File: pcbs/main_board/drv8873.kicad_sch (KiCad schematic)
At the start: 10 parts, among them U3 DRV8873HPWPRQ1

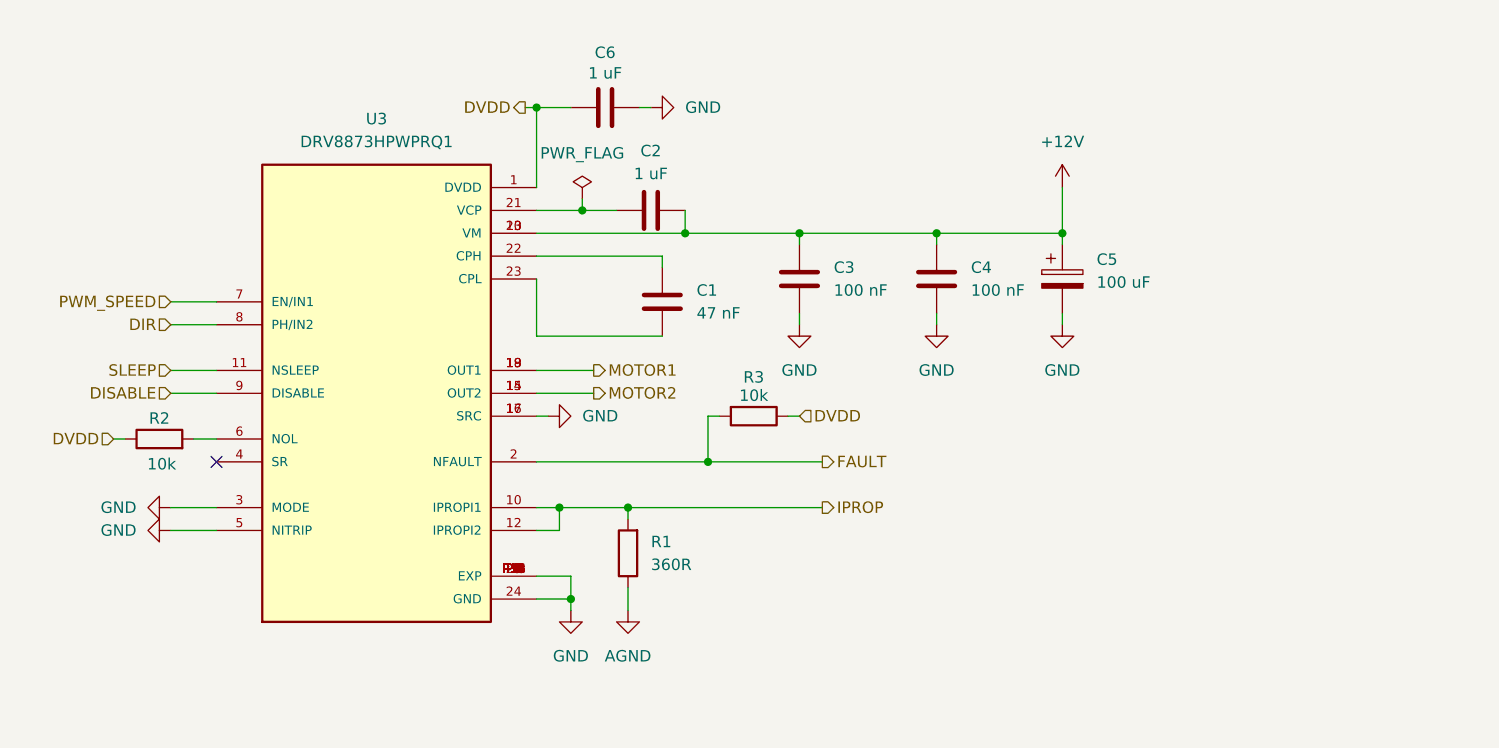
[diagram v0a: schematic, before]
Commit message: Add power distribution sheet
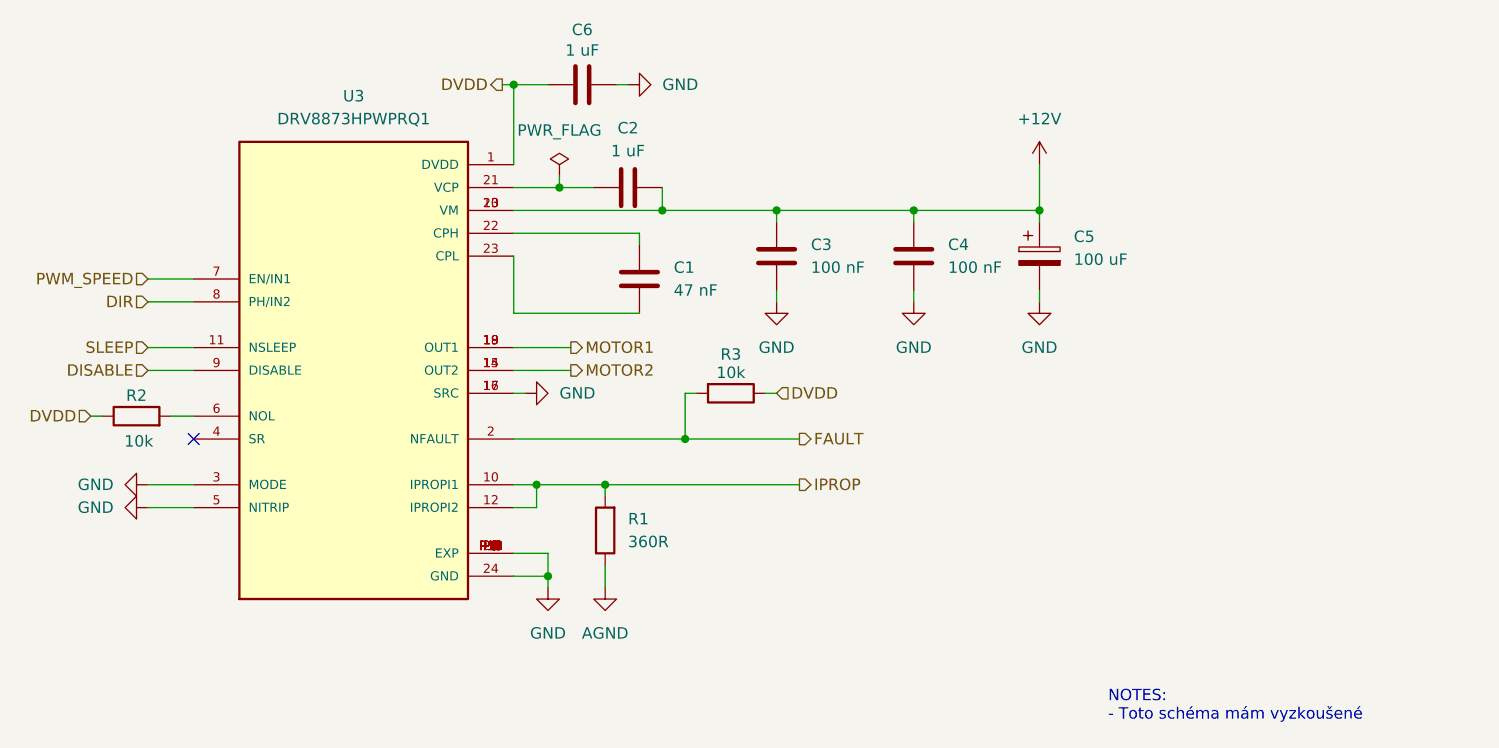
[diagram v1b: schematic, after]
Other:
- note added: "NOTES: - Toto schéma mám vyzkoušené"
- moved on the sheet: C1, C2, C3, C4, C5, C6, R1, R2, R3, U3

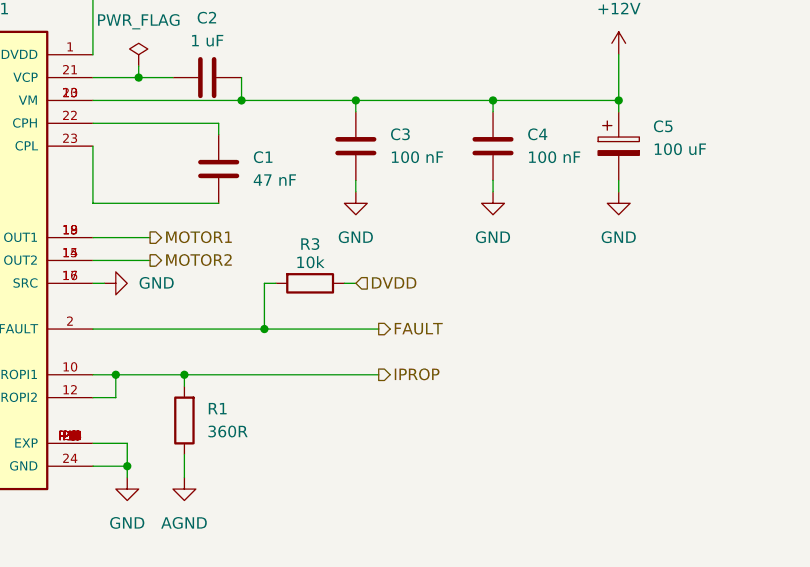
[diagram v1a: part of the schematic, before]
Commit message: wire m driver to esp
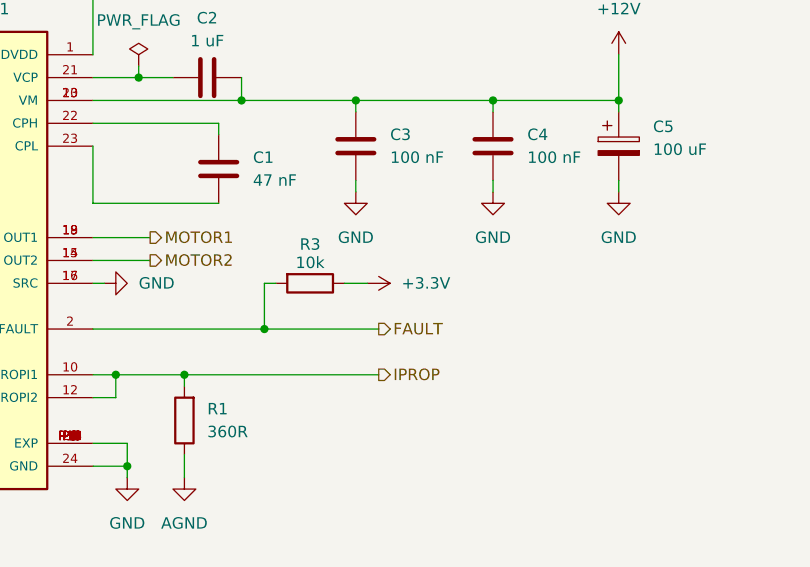
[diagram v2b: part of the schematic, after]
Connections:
- net DVDD: no longer R3.1
- new net +3.3V: R3.1
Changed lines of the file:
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@@
 	(wire
 		(pts
-			(xy 121.92 62.23) (xy 123.19 62.23)
+			(xy 121.92 62.23) (xy 124.46 62.23)
 		)
 		(stroke
@@
 			)
 			(justify right)
-		)
-	)
-	(hierarchical_label "DVDD"
-		(shape input)
-		(at 123.19 62.23 0)
-		(effects
-			(font
-				(size 1.27 1.27)
-			)
-			(justify left)
 		)
 	)
@@
 					(unit 1)
 				)
+			)
+		)
+	)
+	(symbol
+		(lib_id "power:VCC")
+		(at 124.46 62.23 270)
+		(unit 1)
+		(exclude_from_sim no)
+		(in_bom yes)
+		(on_board yes)
+		(dnp no)
+		(fields_autoplaced yes)
+		(property "Reference" "#PWR033"
+			(at 120.65 62.23 0)
+			(effects
+				(font
+					(size 1.27 1.27)
+				)
+				(hide yes)
+			)
+		)
+		(property "Value" "+3.3V"
+			(at 128.27 62.2299 90)
+			(effects
+				(font
+					(size 1.27 1.27)
+				)
+				(justify left)
+			)
+		)
+		(property "Footprint" ""
+			(at 124.46 62.23 0)
+			(effects
+				(font
+					(size 1.27 1.27)
+				)
+				(hide yes)
+			)
+		)
+		(property "Datasheet" ""
+			(at 124.46 62.23 0)
+			(effects
+				(font
+					(size 1.27 1.27)
+				)
+				(hide yes)
+			)
+		)
+		(property "Description" "Power symbol creates a global label with name \"VCC\""
+			(at 124.46 62.23 0)
+			(effects
+				(font
+					(size 1.27 1.27)
+				)
+				(hide yes)
+			)
+		)
+		(pin "1"
+		)
+		(instances
+			(project "main_board"
+				(path "/86b00c07-962a-4c6d-8d05-813891e412c9/42661c25-a76d-41a1-8ad4-79781b4adf06"
+					(reference "#PWR033")
+					(unit 1)
+				)

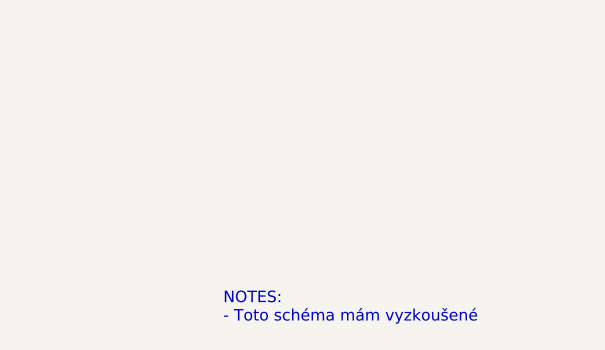
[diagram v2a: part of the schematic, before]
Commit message: ESP power update
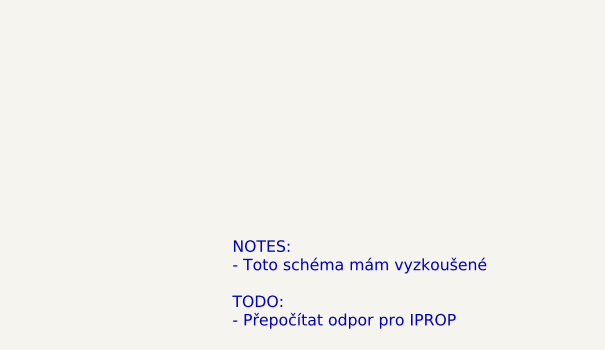
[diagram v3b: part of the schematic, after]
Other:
- note added: "NOTES: - Toto schéma mám vyzkoušené TODO: - Přepočítat odpor pro IPROP"
- note removed: "NOTES: - Toto schéma mám vyzkoušené"
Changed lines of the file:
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@@
 	(generator_version "9.0")
 	(paper "A5")
-	(text "NOTES:\n- Toto schéma mám vyzkoušené"
+	(text "NOTES:\n- Toto schéma mám vyzkoušené\n\nTODO:\n- Přepočítat odpor pro IPROP "
 		(exclude_from_sim no)
-		(at 160.02 95.25 0)
+		(at 161.036 89.662 0)
 		(effects
 			(font

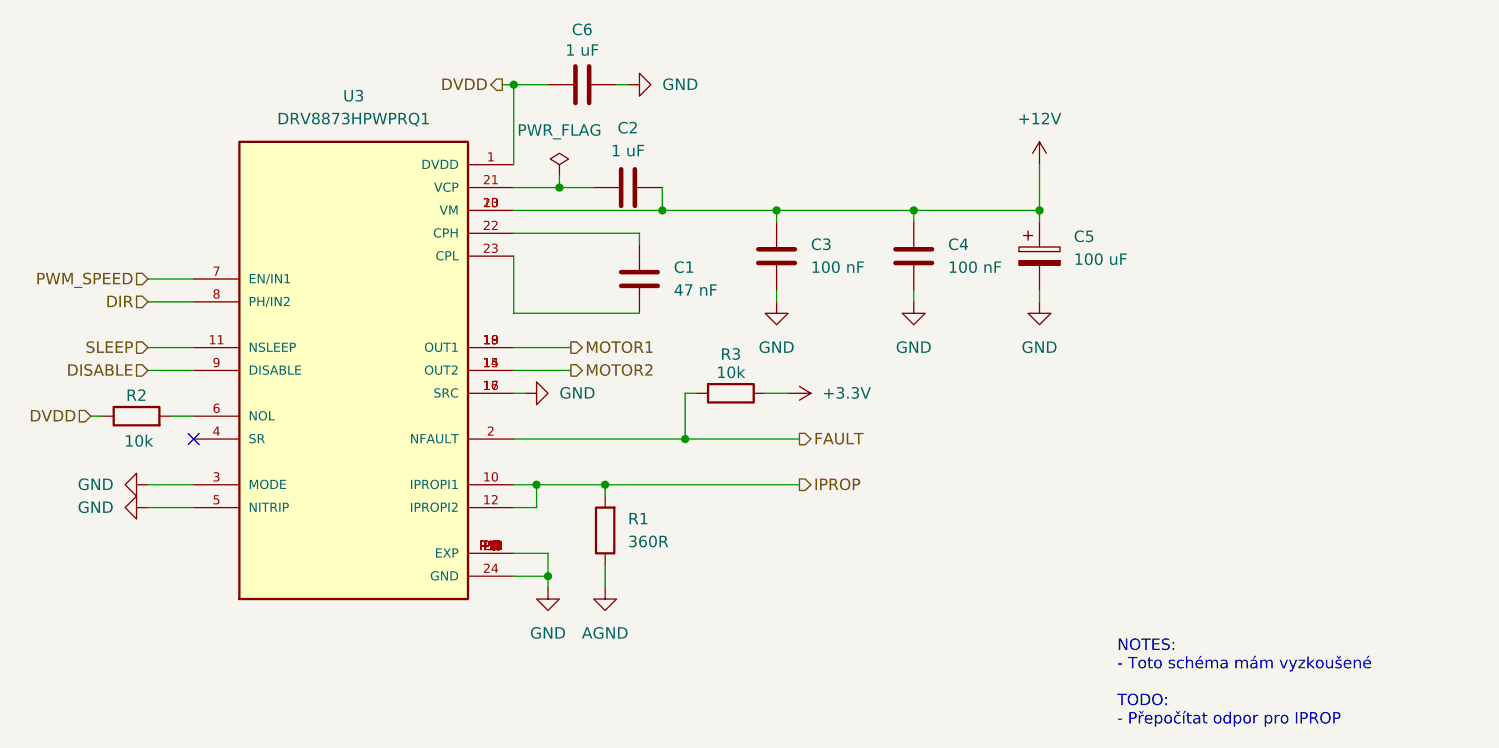
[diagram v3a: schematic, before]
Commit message: Add edge cuts and notes to pcb
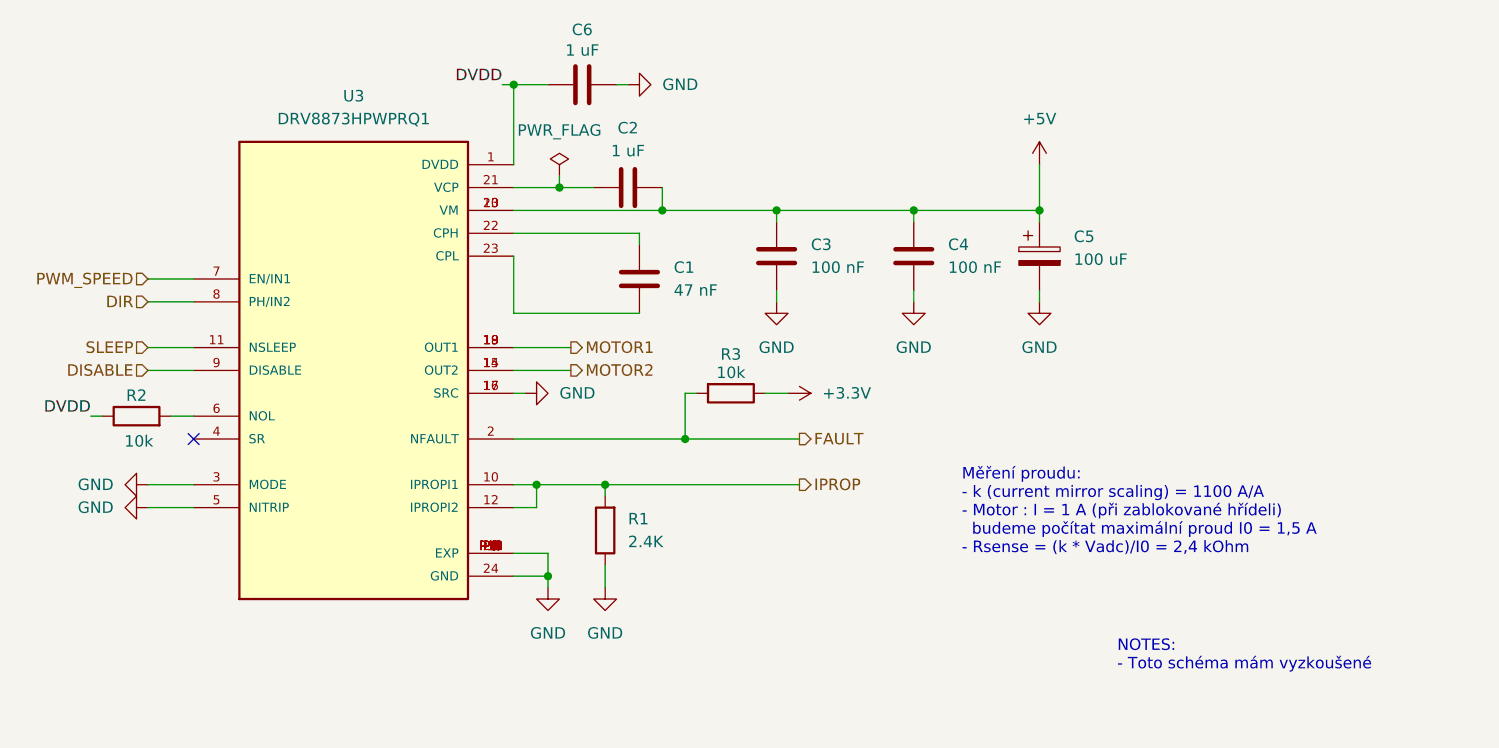
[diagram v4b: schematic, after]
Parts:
- R1: value 360R -> 2.4K; Manufacturer Part Number CRCW0603360RJNTA -> AR0603JR-072K4L; Supplier Part Number 71-CRCW0603J-360 -> 603-AR0603JR-072K4L
- U3: A1_MAX (none) -> None; A1_MIN (none) -> 0.05; A1_NOM (none) -> None; A_MAX (none) -> 1.2; A_MIN (none) -> 1.2; A_NOM (none) -> 1.2; Availability (none) -> In Stock; B_MAX (none) -> 0.3; B_MIN (none) -> 0.19; B_NOM (none) -> 0.245; Check_prices (none) -> https://www.snapeda.com/parts/DRV8873HPWPRQ1/Texas+Instrume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; D2_MAX (none) -> 4.5; D2_MIN (none) -> None; D2_NOM (none) -> None; D_MAX (none) -> 7.9; D_MIN (none) -> 7.7; D_NOM (none) -> 7.8; Description_1 (none) -> Automotive 40-V, 10-A H-bridge motor driver with integrated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; E1_MAX (none) -> 4.5; E1_MIN (none) -> 43.0; E1_NOM (none) -> 23.75; E2_MAX (none) -> 3.0; E2_MIN (none) -> None; E2_NOM (none) -> None; ENOM (none) -> 0.65; E_MAX (none) -> 6.6; E_MIN (none) -> 6.2; E_NOM (none) -> 6.4; L_MAX (none) -> 0.75; L_MIN (none) -> 0.5; L_NOM (none) -> 0.625; MANUFACTURER (none) -> Texas Instruments; MF (none) -> Texas Instruments; MP (none) -> DRV8873HPWPRQ1; PARTREV (none) -> AUG2018; PIN_COUNT (none) -> 24.0; Package (none) -> HTSSOP-24 Texas Instruments; Price (none) -> None; STANDARD (none) -> IPC 7351B; SnapEDA_Link (none) -> https://www.snapeda.com/parts/DRV8873HPWPRQ1/Texas+Instrume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
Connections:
- net AGND is gone; now on net GND: R1.1
- net +12V renamed +5V
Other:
- note added: "Měření proudu: - k (current mirror scaling) = 1100 A/A - Motor : I = 1 A (při zablokované hřídeli) budeme počítat maximální proud I0 = 1,5 A - Rsense = (k * Vadc)/I0 = 2,4 kOhm"
- note added: "NOTES: - Toto schéma mám vyzkoušené"
- note removed: "NOTES: - Toto schéma mám vyzkoušené TODO: - Přepočítat odpor pro IPROP"

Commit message: Components update
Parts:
- U3: A1_MAX None -> (none); A1_MIN 0.05 -> (none); A1_NOM None -> (none); A_MAX 1.2 -> (none); A_MIN 1.2 -> (none); A_NOM 1.2 -> (none); Availability In Stock -> (none); B_MAX 0.3 -> (none); B_MIN 0.19 -> (none); B_NOM 0.245 -> (none); Check_prices https://www.snapeda.com/parts/DRV8873HPWPRQ1/Texas+Instrume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 -> (none); D2_MAX 4.5 -> (none); D2_MIN None -> (none); D2_NOM None -> (none); D_MAX 7.9 -> (none); D_MIN 7.7 -> (none); D_NOM 7.8 -> (none); Description_1 Automotive 40-V, 10-A H-bridge motor driver with integrated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 -> (none); E1_MAX 4.5 -> (none); E1_MIN 43.0 -> (none); E1_NOM 23.75 -> (none); E2_MAX 3.0 -> (none); E2_MIN None -> (none); E2_NOM None -> (none); ENOM 0.65 -> (none); E_MAX 6.6 -> (none); E_MIN 6.2 -> (none); E_NOM 6.4 -> (none); L_MAX 0.75 -> (none); L_MIN 0.5 -> (none); L_NOM 0.625 -> (none); MANUFACTURER Texas Instruments -> (none); MF Texas Instruments -> (none); MP DRV8873HPWPRQ1 -> (none); PARTREV AUG2018 -> (none); PIN_COUNT 24.0 -> (none); Package HTSSOP-24 Texas Instruments -> (none); Price None -> (none); STANDARD IPC 7351B -> (none); SnapEDA_Link https://www.snapeda.com/parts/DRV8873HPWPRQ1/Texas+Instrume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 -> (none)

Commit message: Main board final update
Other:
- note removed: "NOTES: - Toto schéma mám vyzkoušené"
- company: (none) -> Brno Mars Rover
- title: (none) -> Main board - MyMachine LED cap
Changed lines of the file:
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@@
 	(generator "eeschema")
 	(generator_version "9.0")
-	(paper "A5")
+	(paper "A4")
+	(title_block
+		(title "Main board - MyMachine LED cap")
+		(date "2026-01-20")
+		(company "Brno Mars Rover")
+	)
 	(text "Měření proudu:\n- k (current mirror scaling) = 1100 A/A\n- Motor : I = 1 A (při zablokované hřídeli)\n  budeme počítat maximální proud I0 = 1,5 A\n- Rsense = (k * Vadc)/I0 = 2,4 kOhm"
 		(exclude_from_sim no)
@@
 		(effects
 			(font
-				(size 1.27 1.27)
-			)
-			(justify left top)
-		)
-	)
-	(text "NOTES:\n- Toto schéma mám vyzkoušené"
-		(exclude_from_sim no)
-		(at 161.036 89.662 0)
-		(effects
-			(font

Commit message: Fix bom errors - main board
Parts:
- C3, C4: Supplier Part Number 603-CC603KRX7R9BB103 -> 80-C0603C104M5R
- R2, R3: Manufacturer Part Number CRCW0603910KFKEAHP -> CRCW060310K0FKEI; Supplier Part Number 71-CRCW0603910KFKEAH -> 71-CRCW060310K0FKEI
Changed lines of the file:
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@@
 			)
 		)
-		(property "Supplier Part Number" "603-CC603KRX7R9BB103"
+		(property "Supplier Part Number" "80-C0603C104M5R"
 			(at 138.43 46.99 0)
 			(effects
@@
 			)
 		)
-		(property "Manufacturer Part Number" "CRCW0603910KFKEAHP"
+		(property "Manufacturer Part Number" "CRCW060310K0FKEI"
 			(at 118.11 62.23 90)
 			(effects
@@
 			)
 		)
-		(property "Supplier Part Number" "71-CRCW0603910KFKEAH"
+		(property "Supplier Part Number" "71-CRCW060310K0FKEI"
 			(at 118.11 62.23 90)
 			(effects
@@
 			)
 		)
-		(property "Supplier Part Number" "603-CC603KRX7R9BB103"
+		(property "Supplier Part Number" "80-C0603C104M5R"
 			(at 123.19 46.99 0)
 			(effects
@@
 			)
 		)
-		(property "Manufacturer Part Number" "CRCW0603910KFKEAHP"
+		(property "Manufacturer Part Number" "CRCW060310K0FKEI"
 			(at 52.07 64.77 90)
 			(effects
@@
 			)
 		)
-		(property "Supplier Part Number" "71-CRCW0603910KFKEAH"
+		(property "Supplier Part Number" "71-CRCW060310K0FKEI"
 			(at 52.07 64.77 90)
 			(effects
